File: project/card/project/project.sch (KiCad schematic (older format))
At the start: 26 parts

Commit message: schematic design v1
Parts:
- added D?: LED, symbol Device:LED
- added J?: Conn_01x04_Female, symbol Connector:Conn_01x04_Female
- added J?: Conn_01x07_Female, symbol Connector:Conn_01x07_Female
- added LS?: Speaker_Crystal, symbol Device:Speaker_Crystal
- added R?: 220, symbol Device:R
- added SW?: SW_Push_Dual, symbol Switch:SW_Push_Dual
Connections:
- net +3V3: now also J?.2 (Pin_2), SW?.1, SW?.3
- net +5V: now also J?.1 (Pin_1)
- net GND: now also U?.25 (GND), U?.27 (GND), U?.3 (GND), U?.44 (GND), U?.49 (GND), U?.50 (GND), U?.51 (GND), U?.52 (GND), U?.53 (GND), U?.54 (GND), U?.55 (GND), U?.56 (GND), U?.57 (GND), U?.7 (GND), D?.1 (K), J?.1 (Pin_1), J?.4 (Pin_4), LS?.2
- net at U?.14 (PB15/SPI2_MOSI): now also J?.4 (Pin_4)
- net at U?.16 (PB13/SPI2_SCK): now also J?.3 (Pin_3)
- net NSS: now reaches U?.17 (PB12/SPI2_NSS)
- net NSS: now also J?.7 (Pin_7)
- net echo: now reaches U?.21 (PA5/ADC5/DAC2)
- net echo: now also R?.1
- net trig: now reaches U?.22 (PA4/ADC4/DAC1)
- net trig: now also J?.2 (Pin_2)
- net Reset: now reaches U?.35 (PB8/I2C1_SCL)
- net Reset: now also J?.5 (Pin_5)
- net DataCom: now reaches U?.36 (PB9/I2C1_SDA)
- net DataCom: now also J?.6 (Pin_6)
- net Btn: now reaches U?.37 (PB2/LPTIM1_OUT)
- net Btn: now also SW?.2, SW?.4
- net LED: now reaches U?.39 (PB6/LPTIM1_ETR)
- net LED: now also D?.2 (A)
- net Piezo: now reaches U?.40 (PB5/LPTIM1_IN1)
- net Piezo: now also LS?.1
- new net: J?.3 (Pin_3), R?.2

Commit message: began work with footprints
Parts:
- removed C? (x2): C, symbol Device:C
- removed R?: 220, symbol Device:R
- C1, C11, C12, C15, C2, C3, C5, C6, C7, C9: renamed from C?; footprint (none) -> Capacitor_SMD:C_0805_2012Metric_Pad1.15x1.40mm_HandSolder
- C13, C4, C8: renamed from C?; footprint (none) -> Capacitor_SMD:CP_Elec_5x4.5
- D1: renamed from D?; footprint (none) -> LED_SMD:LED_2512_6332Metric_Pad1.52x3.35mm_HandSolder
- R1, R2, R3: renamed from R?; footprint (none) -> Resistor_SMD:R_0805_2012Metric_Pad1.15x1.40mm_HandSolder
- gave numbers to parts that had none: 12
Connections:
- net +3V3: now also J7.1 (Pin_1)
- net +5V: no longer J7.1 (Pin_1)
- net echo: now also J7.3 (Pin_3)

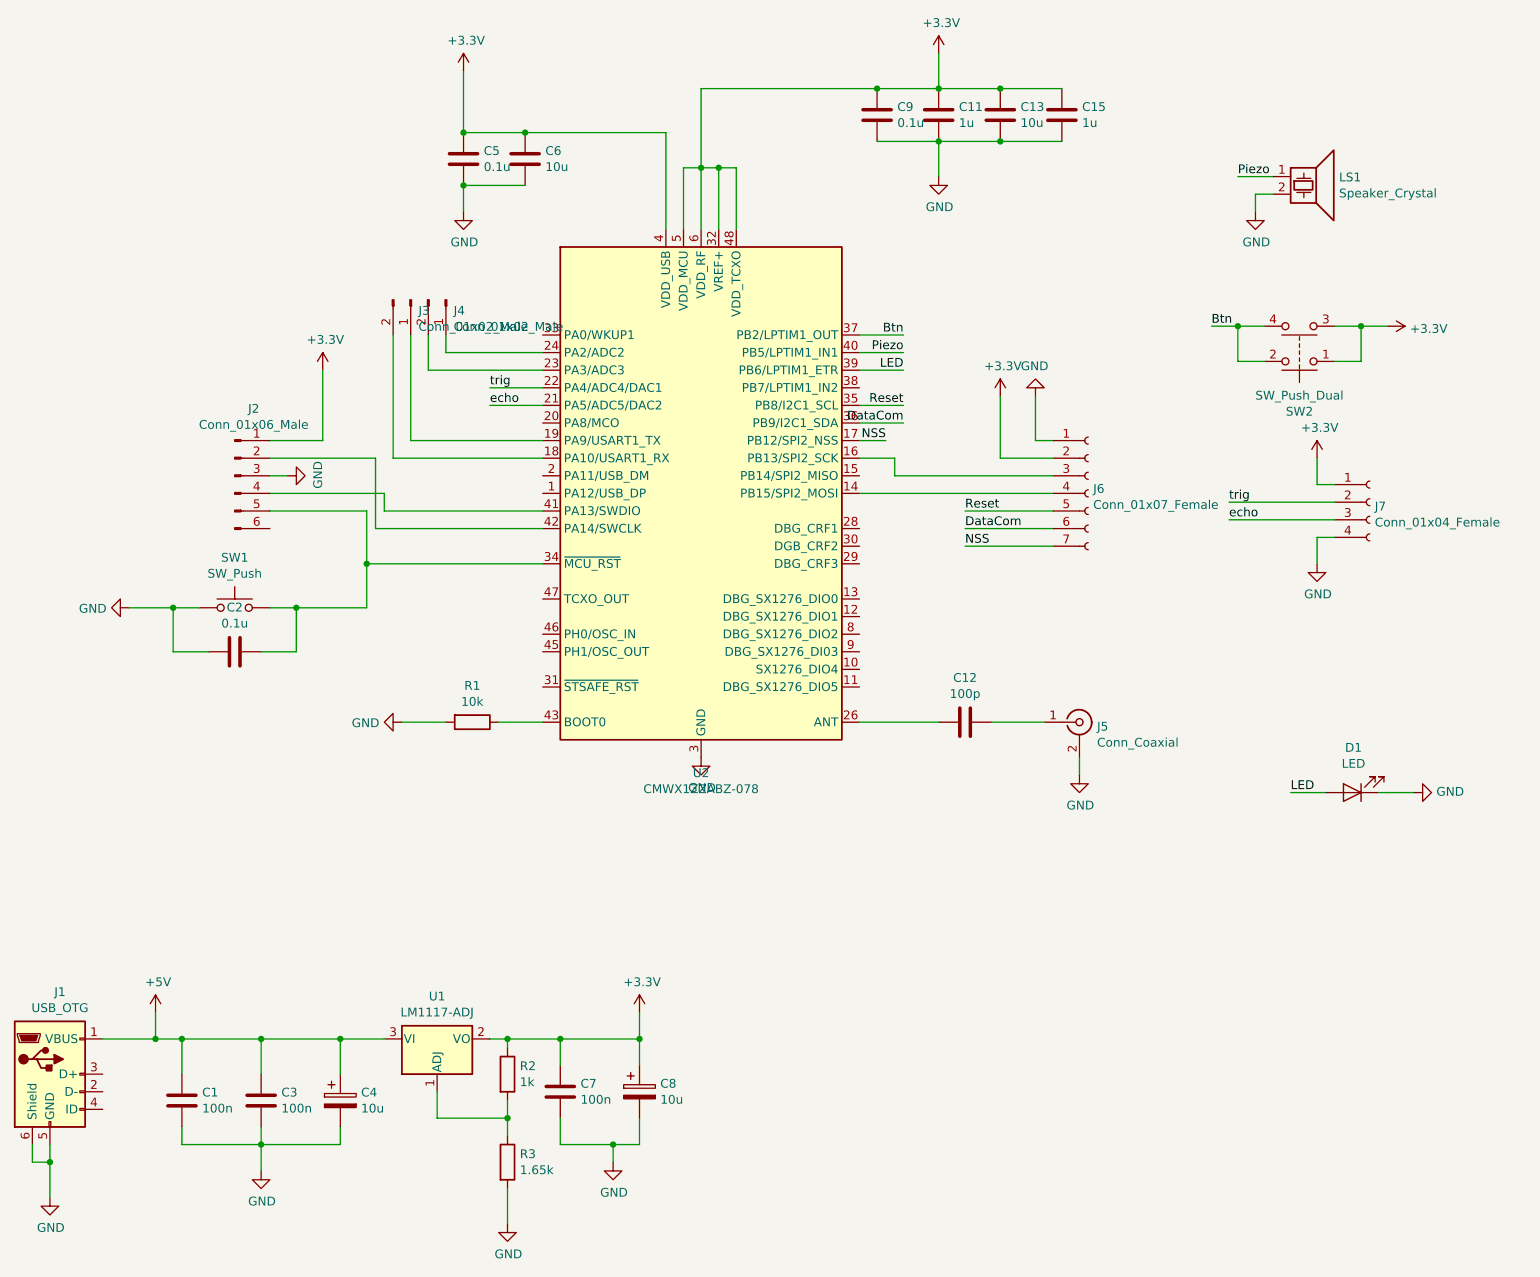
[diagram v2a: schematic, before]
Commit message: add all footprints
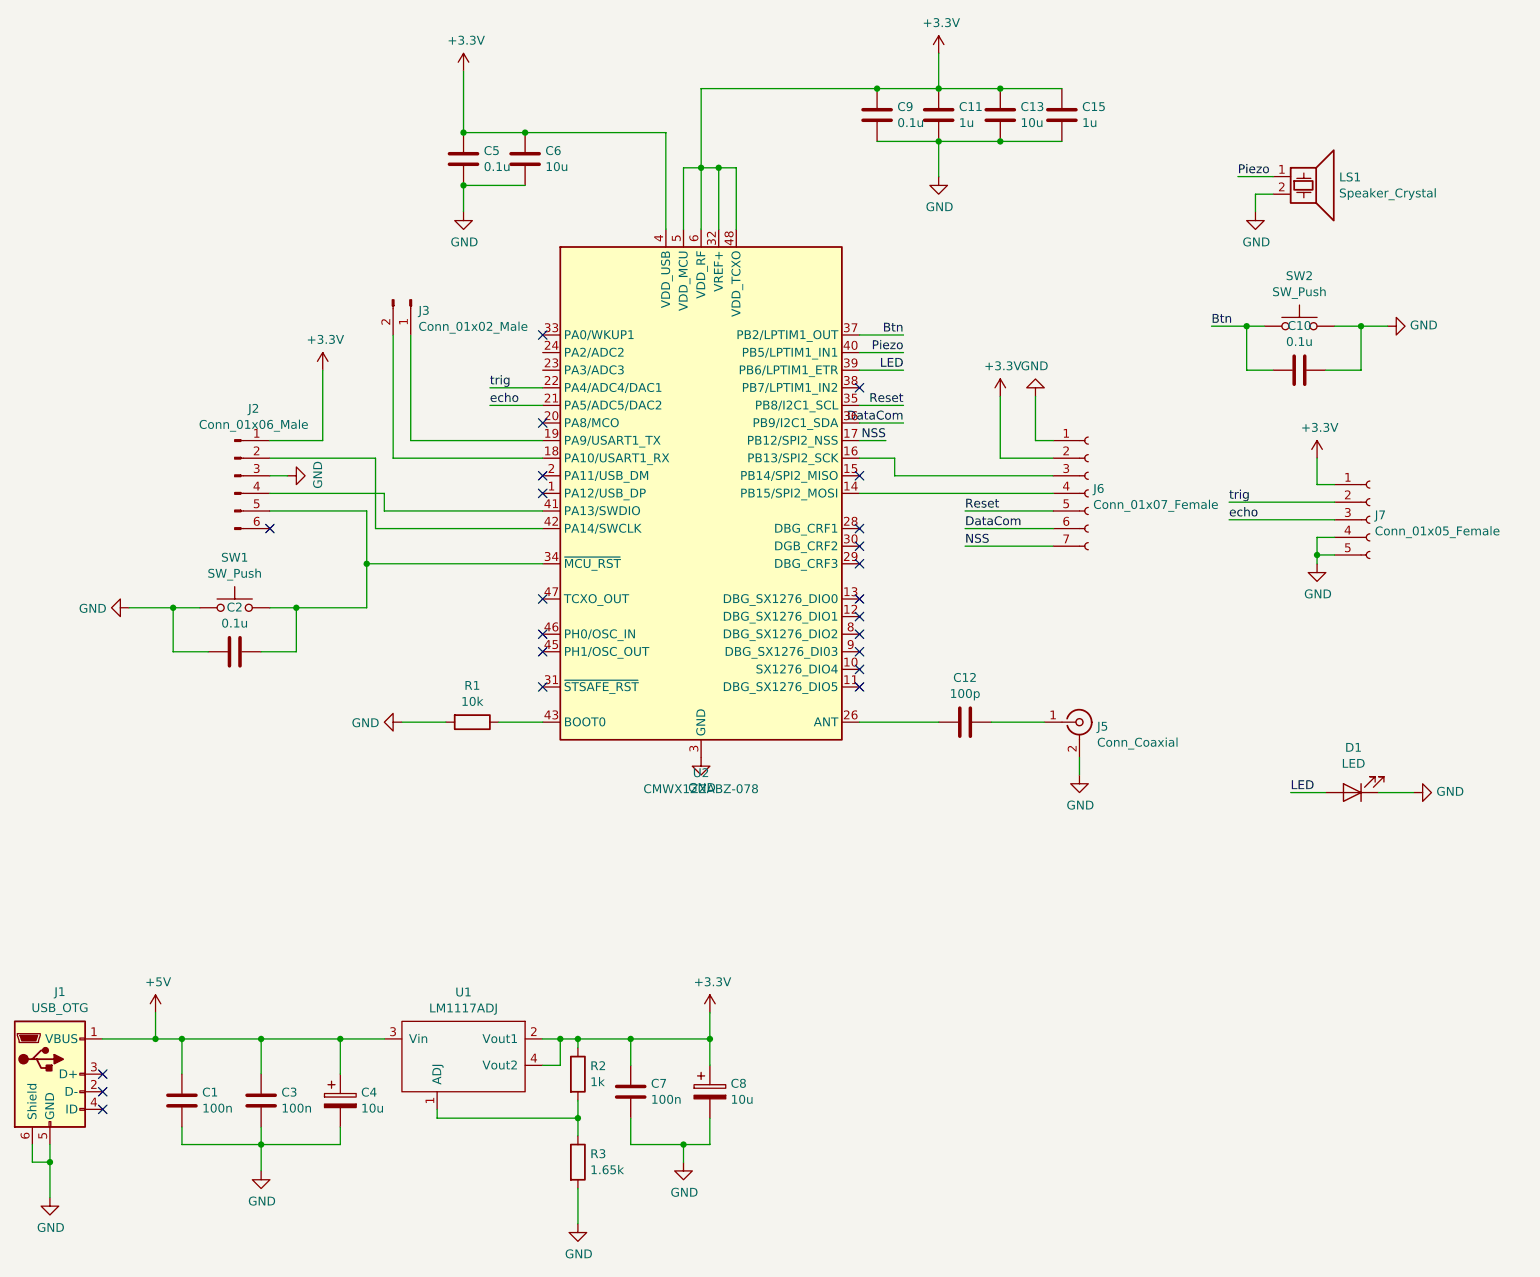
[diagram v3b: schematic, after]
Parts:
- removed J4: Conn_01x02_Male, symbol Connector:Conn_01x02_Male
- removed J7: Conn_01x04_Female, symbol Connector:Conn_01x04_Female
- removed SW2: SW_Push_Dual, symbol Switch:SW_Push_Dual
- removed U1: LM1117-ADJ, symbol Regulator_Linear:LM1117-ADJ
- added C10: 0.1u, Capacitor_SMD:C_0805_2012Metric_Pad1.15x1.40mm_HandSolder, symbol Device:C
- added J7: Conn_01x05_Female, Connector_Molex:Molex_KK-254_AE-6410-05A_1x05_P2.54mm_Vertical, symbol Connector:Conn_01x05_Female
- added SW2: SW_Push, Button_Switch_SMD:SW_Push_1P1T_NO_6x6mm_H9.5mm, symbol Switch:SW_Push
- added U1: LM1117ADJ, Package_TO_SOT_SMD:SOT-223, symbol LM1117ADJ:LM1117ADJ
- D1: footprint LED_SMD:LED_2512_6332Metric_Pad1.52x3.35mm_HandSolder -> LED_SMD:LED_0805_2012Metric_Pad1.15x1.40mm_HandSolder
- J1: footprint (none) -> Connector_USB:USB_Micro-B_Wuerth_629105150521
- J2: footprint (none) -> Connector_Molex:Molex_KK-254_AE-6410-06A_1x06_P2.54mm_Vertical
- J3: footprint (none) -> Connector_Molex:Molex_KK-254_AE-6410-02A_1x02_P2.54mm_Vertical
- J5: footprint (none) -> Connector_Coaxial:U.FL_Molex_MCRF_73412-0110_Vertical
- J6: footprint (none) -> Connector_Molex:Molex_KK-254_AE-6410-07A_1x07_P2.54mm_Vertical
- LS1: footprint (none) -> Buzzer_Beeper:Buzzer_15x7.5RM7.6
- SW1: footprint (none) -> Button_Switch_SMD:SW_Push_1P1T_NO_6x6mm_H9.5mm
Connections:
- net +3V3: now also J7.1 (Pin_1), U1.2 (Vout1), U1.4 (Vout2)
- net +5V: now also U1.3 (Vin)
- net Btn: now also C10.2, SW2.1
- net GND: now also C10.1, J7.4 (Pin_4), J7.5 (Pin_5), SW2.2
- net echo: now also J7.3 (Pin_3)
- net trig: now also J7.2 (Pin_2)
- net at R2.2, R3.1: now also U1.1 (ADJ)
- no-connect marks 0 -> 23
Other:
- moved on the sheet: C7, C8, R2, R3

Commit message: layout etc
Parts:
- added C14, C16: _, Capacitor_SMD:C_0805_2012Metric_Pad1.15x1.40mm_HandSolder, symbol Device:C
- added D2: LED, LED_SMD:LED_0805_2012Metric_Pad1.15x1.40mm_HandSolder, symbol Device:LED
- added R4: 660, Resistor_SMD:R_0805_2012Metric_Pad1.15x1.40mm_HandSolder, symbol Device:R
- added R5: 220, Resistor_SMD:R_0805_2012Metric_Pad1.15x1.40mm_HandSolder, symbol Device:R
- C13: footprint Capacitor_SMD:CP_Elec_5x4.5 -> Capacitor_SMD:C_0805_2012Metric_Pad1.15x1.40mm_HandSolder
- J2: footprint Connector_Molex:Molex_KK-254_AE-6410-06A_1x06_P2.54mm_Vertical -> Connector_PinHeader_2.54mm:PinHeader_1x06_P2.54mm_Vertical
- J3: footprint Connector_Molex:Molex_KK-254_AE-6410-02A_1x02_P2.54mm_Vertical -> Connector_PinHeader_2.54mm:PinHeader_1x02_P2.54mm_Vertical
- J6: footprint Connector_Molex:Molex_KK-254_AE-6410-07A_1x07_P2.54mm_Vertical -> Connector_PinSocket_2.54mm:PinSocket_1x07_P2.54mm_Vertical
- J7: footprint Connector_Molex:Molex_KK-254_AE-6410-05A_1x05_P2.54mm_Vertical -> Connector_PinSocket_2.54mm:PinSocket_1x05_P2.54mm_Vertical
- U2: footprint RF_Module:CMWX1ZZABZ -> test:CMWX1ZZABZ
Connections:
- net +3V3: now also R4.2
- net GND: now also C14.2, C16.2, D2.1 (K)
- net LED: now also R5.2; no longer D1.2 (A)
- net at C12.2, U2.26 (ANT): now also C14.1
- net at C12.1, J5.1 (In): now also C16.1
- new net: D1.2 (A), R5.1
- new net: D2.2 (A), R4.1
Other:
- note added: "150mA"
- note added: "200mA\n"
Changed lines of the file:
@@
 F 0 "U2" H 5500 1611 50  0000 C CNN
 F 1 "CMWX1ZZABZ-078" H 5500 1520 50  0000 C CNN
-F 2 "RF_Module:CMWX1ZZABZ" H 5500 3200 50  0001 C CNN
+F 2 "test:CMWX1ZZABZ" H 5500 3200 50  0001 C CNN
 F 3 "https://wireless.murata.com/RFM/data/type_abz.pdf" H 7950 1700 50  0001 C CNN
 	1    5500 3200
@@
 F 0 "C13" H 7315 1096 50  0000 L CNN
 F 1 "10u" H 7315 1005 50  0000 L CNN
-F 2 "Capacitor_SMD:CP_Elec_5x4.5" H 7238 900 50  0001 C CNN
+F 2 "Capacitor_SMD:C_0805_2012Metric_Pad1.15x1.40mm_HandSolder" H 7238 900 50  0001 C CNN
 F 3 "~" H 7200 1050 50  0001 C CNN
 	1    7200 1050
@@
 F 0 "J2" H 2958 3481 50  0000 C CNN
 F 1 "Conn_01x06_Male" H 2958 3390 50  0000 C CNN
-F 2 "Connector_Molex:Molex_KK-254_AE-6410-06A_1x06_P2.54mm_Vertical" H 2850 3100 50  0001 C CNN
+F 2 "Connector_PinHeader_2.54mm:PinHeader_1x06_P2.54mm_Vertical" H 2850 3100 50  0001 C CNN
 F 3 "~" H 2850 3100 50  0001 C CNN
 	1    2850 3100
@@
 F 0 "J3" V 3912 2144 50  0000 L CNN
 F 1 "Conn_01x02_Male" V 4003 2144 50  0000 L CNN
-F 2 "Connector_Molex:Molex_KK-254_AE-6410-02A_1x02_P2.54mm_Vertical" H 3850 2100 50  0001 C CNN
+F 2 "Connector_PinHeader_2.54mm:PinHeader_1x02_P2.54mm_Vertical" H 3850 2100 50  0001 C CNN
 F 3 "~" H 3850 2100 50  0001 C CNN
 	1    3850 2100
@@
 F 0 "J6" H 7728 3226 50  0000 L CNN
 F 1 "Conn_01x07_Female" H 7728 3135 50  0000 L CNN
-F 2 "Connector_Molex:Molex_KK-254_AE-6410-07A_1x07_P2.54mm_Vertical" H 7700 3200 50  0001 C CNN
+F 2 "Connector_PinSocket_2.54mm:PinSocket_1x07_P2.54mm_Vertical" H 7700 3200 50  0001 C CNN
 F 3 "~" H 7700 3200 50  0001 C CNN
 	1    7700 3200
@@
 	0    -1   -1   0
 $EndComp
-Text Label 8850 4900 0    50   ~ 0
+Text Label 8350 4900 0    50   ~ 0
 LED
 Text Label 8400 2250 0    50   ~ 0
@@
 	7650 4800 7650 4700
 Wire Wire Line
-	7150 4500 7450 4500
-Wire Wire Line
-	6400 4500 6850 4500
+	7150 4500 7250 4500
+Wire Wire Line
+	6400 4500 6700 4500
 $Comp
 L power:+3.3V #PWR0116
@@
 F 0 "J7" H 9328 3376 50  0000 L CNN
 F 1 "Conn_01x05_Female" H 9328 3285 50  0000 L CNN
-F 2 "Connector_Molex:Molex_KK-254_AE-6410-05A_1x05_P2.54mm_Vertical" H 9300 3350 50  0001 C CNN
+F 2 "Connector_PinSocket_2.54mm:PinSocket_1x05_P2.54mm_Vertical" H 9300 3350 50  0001 C CNN
 F 3 "~" H 9300 3350 50  0001 C CNN
 	1    9300 3350
@@
 Text Label 4300 2600 0    50   ~ 0
 trig
+$Comp
+L Device:C C14
+U 1 1 5E4736A2
+P 6700 4800
+F 0 "C14" H 6815 4846 50  0000 L CNN
+F 1 "_" H 6815 4755 50  0000 L CNN
+F 2 "Capacitor_SMD:C_0805_2012Metric_Pad1.15x1.40mm_HandSolder" H 6738 4650 50  0001 C CNN
+F 3 "~" H 6700 4800 50  0001 C CNN
+	1    6700 4800
+	1    0    0    -1
+$EndComp
+$Comp
+L Device:C C16
+U 1 1 5E473E2E
+P 7250 4800
+F 0 "C16" H 7365 4846 50  0000 L CNN
+F 1 "_" H 7365 4755 50  0000 L CNN
+F 2 "Capacitor_SMD:C_0805_2012Metric_Pad1.15x1.40mm_HandSolder" H 7288 4650 50  0001 C CNN
+F 3 "~" H 7250 4800 50  0001 C CNN
+	1    7250 4800
+	1    0    0    -1
+$EndComp
+Wire Wire Line
+	7250 4650 7250 4500
+Connection ~ 7250 4500
+Wire Wire Line
+	7250 4500 7450 4500
+Wire Wire Line
+	6700 4500 6700 4650
+Connection ~ 6700 4500
+Wire Wire Line
+	6700 4500 6850 4500
+$Comp
+L power:GND #PWR0124
+U 1 1 5E47E2D0
+P 6700 5150
+F 0 "#PWR0124" H 6700 4900 50  0001 C CNN
+F 1 "GND" H 6705 4977 50  0000 C CNN
+F 2 "" H 6700 5150 50  0001 C CNN
+F 3 "" H 6700 5150 50  0001 C CNN
+	1    6700 5150
+	1    0    0    -1
+$EndComp
+$Comp
+L power:GND #PWR0125
+U 1 1 5E47E840
+P 7250 5150
+F 0 "#PWR0125" H 7250 4900 50  0001 C CNN
+F 1 "GND" H 7255 4977 50  0000 C CNN
+F 2 "" H 7250 5150 50  0001 C CNN
+F 3 "" H 7250 5150 50  0001 C CNN
+	1    7250 5150
+	1    0    0    -1
+$EndComp
+Wire Wire Line
+	7250 5150 7250 4950
+Wire Wire Line
+	6700 4950 6700 5150
+Text Notes 8800 1200 0    50   ~ 0
+150mA
+Text Notes 4800 4750 0    50   ~ 0
+200mA\n
+$Comp
+L Device:R R5
+U 1 1 5E4AC591
+P 8700 4900
+F 0 "R5" V 8493 4900 50  0000 C CNN
+F 1 "220" V 8584 4900 50  0000 C CNN
+F 2 "Resistor_SMD:R_0805_2012Metric_Pad1.15x1.40mm_HandSolder" V 8630 4900 50  0001 C CNN
+F 3 "~" H 8700 4900 50  0001 C CNN
+	1    8700 4900
+	0    1    1    0
+$EndComp
+Wire Wire Line
+	8550 4900 8350 4900
+$Comp
+L Device:LED D2
+U 1 1 5E4BB240
+P 6200 6600
+F 0 "D2" H 6193 6345 50  0000 C CNN
+F 1 "LED" H 6193 6436 50  0000 C CNN
+F 2 "LED_SMD:LED_0805_2012Metric_Pad1.15x1.40mm_HandSolder" H 6200 6600 50  0001 C CNN
+F 3 "~" H 6200 6600 50  0001 C CNN
+	1    6200 6600
+	0    -1   -1   0
+$EndComp
+Text Label 5750 6550 0    50   ~ 0
+LED
+$Comp
+L Device:R R4
+U 1 1 5E4BB249
+P 6050 6300
+F 0 "R4" V 5843 6300 50  0000 C CNN
+F 1 "660" V 5934 6300 50  0000 C CNN
+F 2 "Resistor_SMD:R_0805_2012Metric_Pad1.15x1.40mm_HandSolder" V 5980 6300 50  0001 C CNN
+F 3 "~" H 6050 6300 50  0001 C CNN
+	1    6050 6300
+	0    1    1    0
+$EndComp
+Wire Wire Line
+	5800 6400 5600 6400
+Wire Wire Line
+	6200 6450 6200 6300
+Wire Wire Line
+	5900 6300 5550 6300
+Wire Wire Line
+	5550 6900 6200 6900
+Wire Wire Line
+	6200 6900 6200 6750
+Connection ~ 5550 6900
 $EndSCHEMATC
